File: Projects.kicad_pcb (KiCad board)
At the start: 2 copper layers, 83 x 64 mm, 16 parts, among them P1 7-215079-4, P2 7-215079-4, SW1 SW_Push, SW2 SW_Push, SW3 SW_Push, U1 MAX30102, U2 SSD1306

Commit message: feat: Se agrega el archivo .gitignore mas cambios en sch y pcb
Se agregan los archivos mencionados en el titulo
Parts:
- added J1: Conn_01x03_Pin, Connector_JST:JST_EH_B3B-EH-A_1x03_P2.50mm_Vertical, F.Cu at (74.3, 114.9)
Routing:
- net +5V: track 52.6 -> 89.7 mm, vias 0 -> 2

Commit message: feat: Se termina de rutear el pcb
Se termina de rutear el pcb
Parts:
- moved SW1 7.87 mm to (131.4, 67.3), turned to -90 degrees
- moved J1 3.28 mm to (71.1, 115.6)
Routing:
- net +5V: track 89.7 -> 196.6 mm, vias 2 -> 8
- net /SCL: track 57.8 -> 126.3 mm, vias 1 -> 5
- net Net-(A1-D4): track 0.00 -> 46.2 mm, vias 0 -> 2
- net Net-(A1-D2): track 0.00 -> 43.3 mm, vias 0 -> 2
- net Net-(A1-D3): track 0.00 -> 37.9 mm, vias 0 -> 1
- net /SDA: track 115.4 -> 151.1 mm, vias 1 -> 3
- net Net-(A1-D12): track 0.00 -> 10.2 mm, vias 0 -> 1
- net Net-(D1-A): track 0.00 -> 3.81 mm

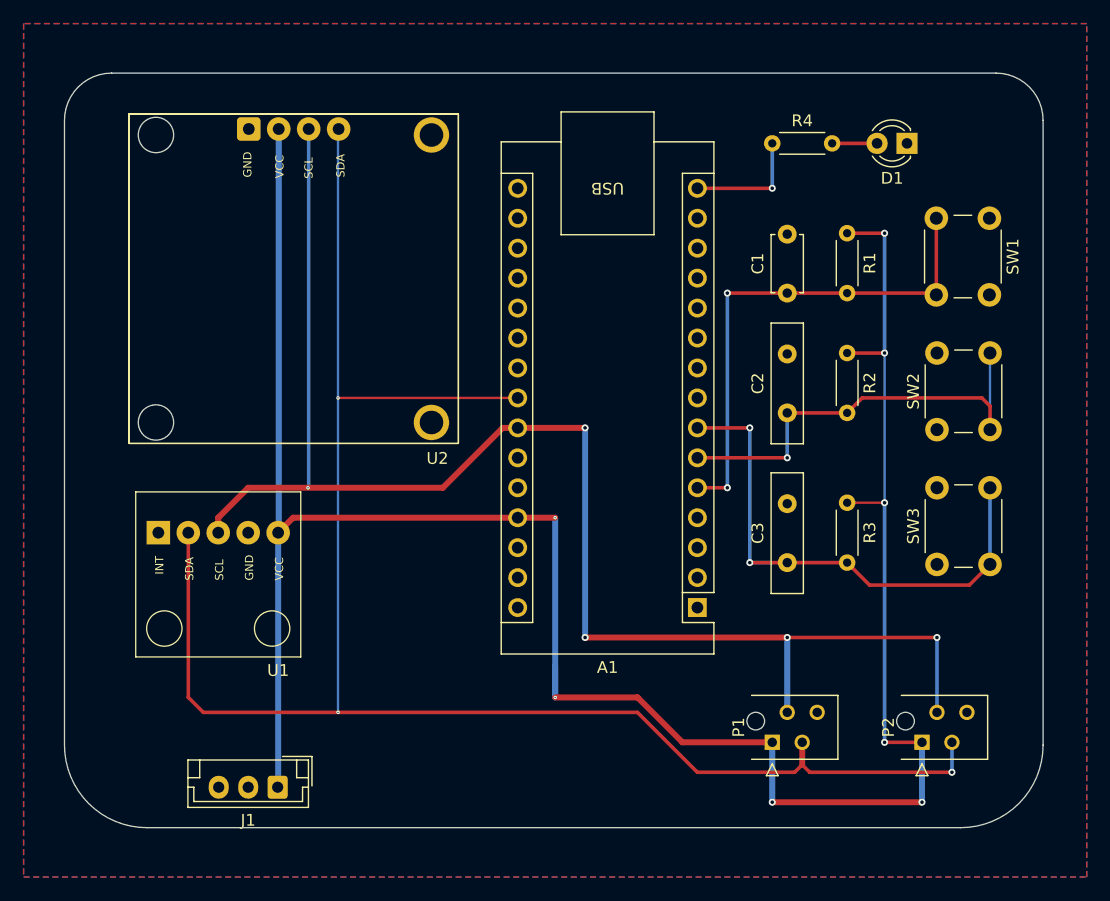
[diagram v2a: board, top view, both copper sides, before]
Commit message: feat: Generacion de archivos gerber
Se termina el diseño del entrenamiento y se generan los archivos gerber
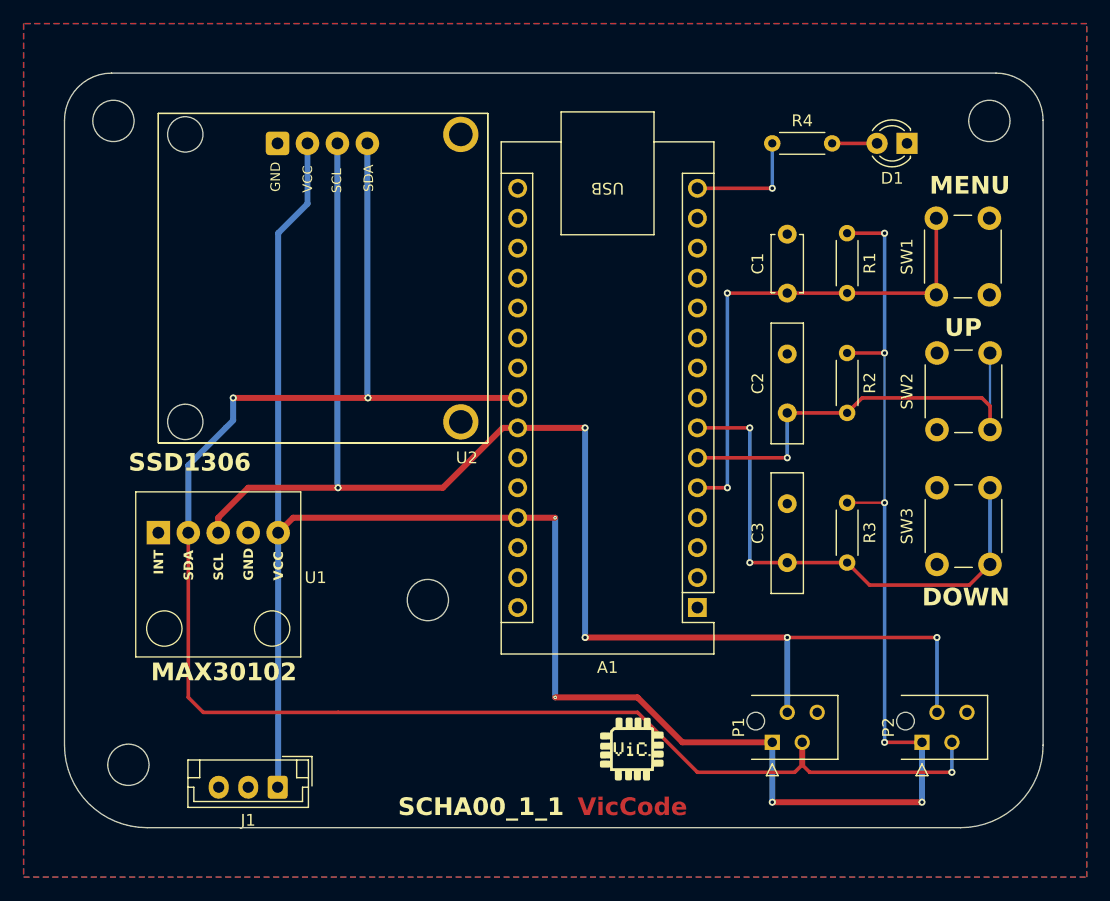
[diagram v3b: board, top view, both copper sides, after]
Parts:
- added G***: LOGO, LOGO, F.Cu at (101.0, 112.4)
- added REF**: MountingHole_3.5mm, MountingHole:MountingHole_3.5mm, F.Cu at (58.4, 113.7)
- added REF**: MountingHole_3.5mm, MountingHole:MountingHole_3.5mm, F.Cu at (131.4, 59.1)
- added REF**: MountingHole_3.5mm, MountingHole:MountingHole_3.5mm, F.Cu at (57.1, 59.1)
- added REF**: MountingHole_3.5mm, MountingHole:MountingHole_3.5mm, F.Cu at (83.8, 99.7)
- moved U2 2.49 mm to (74.9, 72.4)
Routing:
- net /SDA: track 151.1 -> 145.1 mm
- net +5V: track 196.6 -> 193.8 mm
- net Net-(A1-D4): track 46.2 -> 44.3 mm
- net /SCL: track 126.3 -> 125.1 mm
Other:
- board text added: "DOWN"
- board text added: "MAX30102"
- board text added: "MENU"
- board text added: "SCHA00_1_1"
- board text added: "SSD1306"
- board text added: "UP"
- board text added: "VicCode"
